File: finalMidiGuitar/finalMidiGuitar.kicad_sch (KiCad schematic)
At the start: 12 parts, among them J1 PinHeader_01x06_P2.54mm_Verti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, J2 PinHeader_01x06_P2.54mm_Verti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, J3 NeoPixel, J4 Oled Display, M1 Module_XIAO_Generic_SocketSMD, SW1 BTN, U1 SN74LVC1T45DBVR

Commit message: Add sensor interrupt handling and enhance button functionality for context-sensitive actions
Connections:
- net at SW1.2: now also M1.3 (D2); no longer M1.8 (D7)
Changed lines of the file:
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@@
+	)
+	(no_connect
+		(at 110.49 101.6)
 	)
 	(no_connect
 		(at 110.49 86.36)
 	)
-	(no_connect
-		(at 110.49 88.9)
-	)
 	(wire
 		(pts
@@
 	(wire
 		(pts
+			(xy 110.49 88.9) (xy 95.25 88.9)
+		)
+		(stroke
+			(width 0)
+			(type default)
+		)
+	)
+	(wire
+		(pts
 			(xy 151.13 152.4) (xy 193.04 152.4)
 		)
@@
 	(wire
 		(pts
-			(xy 95.25 77.47) (xy 95.25 101.6)
-		)
-		(stroke
-			(width 0)
-			(type default)
-		)
-	)
-	(wire
-		(pts
 			(xy 35.56 133.35) (xy 35.56 106.68)
 		)
@@
 	(wire
 		(pts
+			(xy 95.25 88.9) (xy 95.25 77.47)
+		)
+		(stroke
+			(width 0)
+			(type default)
+		)
+	)
+	(wire
+		(pts
 			(xy 218.44 93.98) (xy 218.44 96.52)
 		)
@@
 		)
 	)
-	(wire
-		(pts
-			(xy 95.25 101.6) (xy 110.49 101.6)
-		)
-		(stroke
-			(width 0)
-			(type default)
-		)
-	)

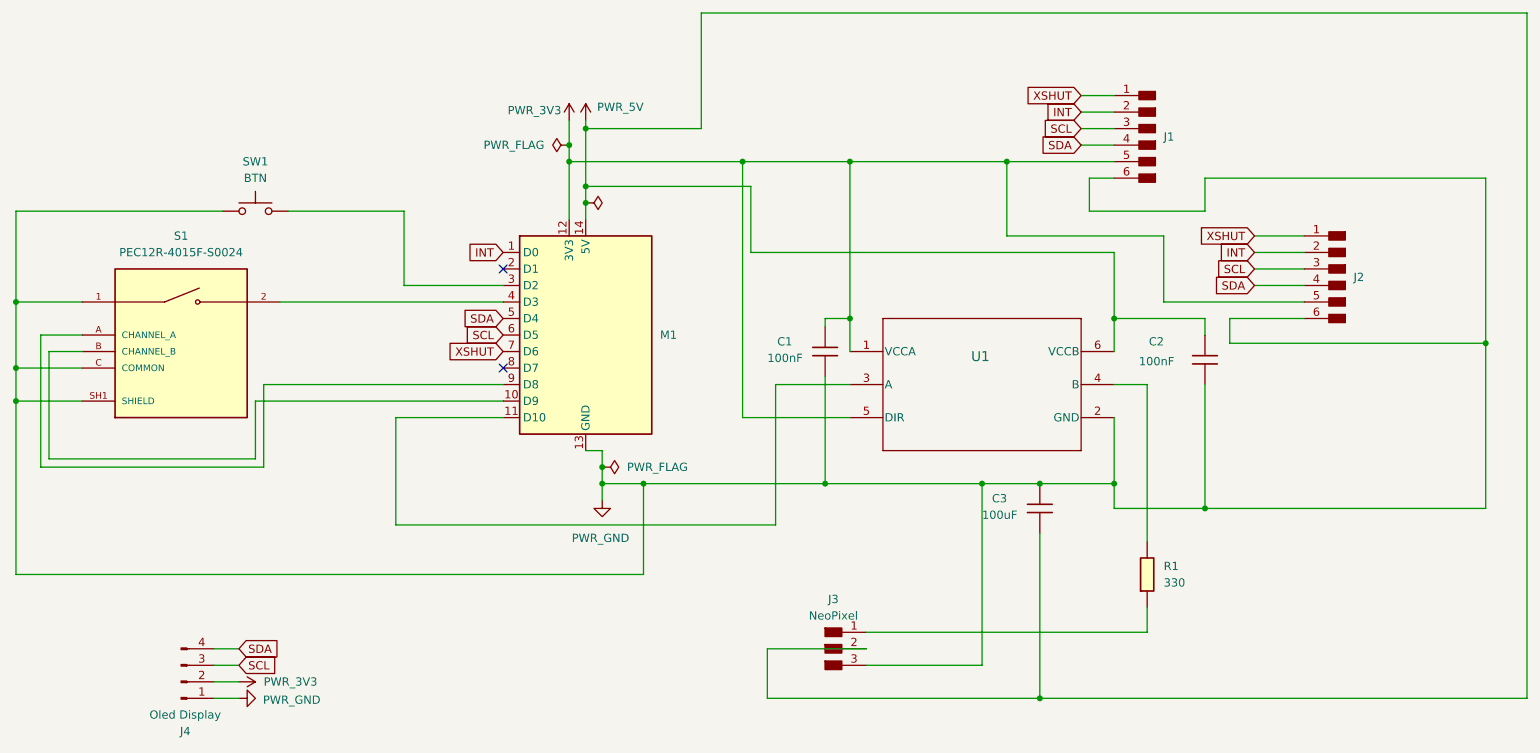
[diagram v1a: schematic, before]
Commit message: Update pad dimensions and clean up schematic and pcb
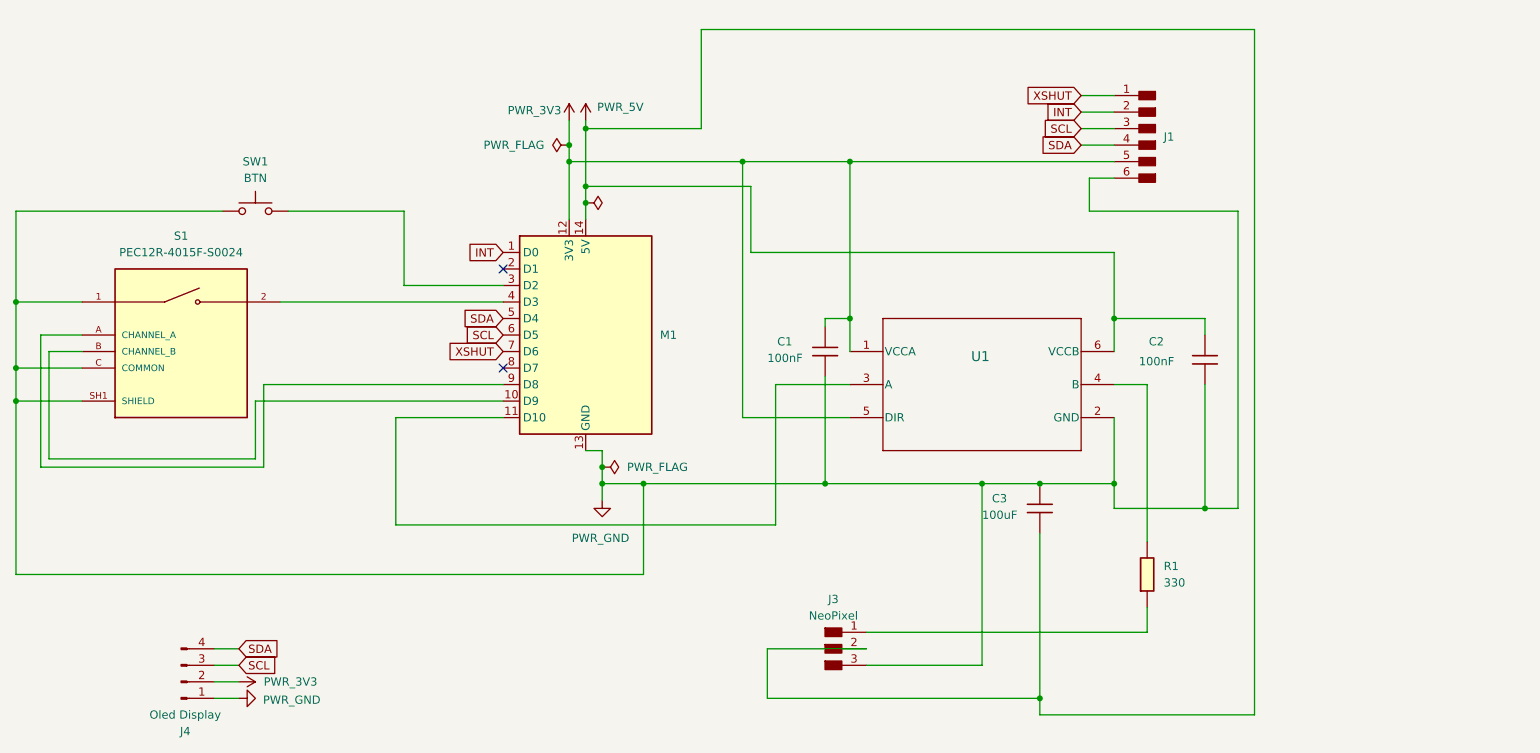
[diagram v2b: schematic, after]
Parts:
- removed J2: PinHeader_01x06_P2.54mm_Vertical_THT_D1mm, PCM_fab:PinHeader_01x06_P2.54mm_Vertical_THT_D1mm, symbol PCM_fab:PinHeader_01x06_P2.54mm_Vertical_THT_D1mm
